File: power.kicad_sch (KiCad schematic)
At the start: 20 parts, among them J3 Life Makes Lemonade, J4 Conn_02x02_Odd_Even, U11 TPS62913, U12 TPS62143RGTR, U13 TPS22993

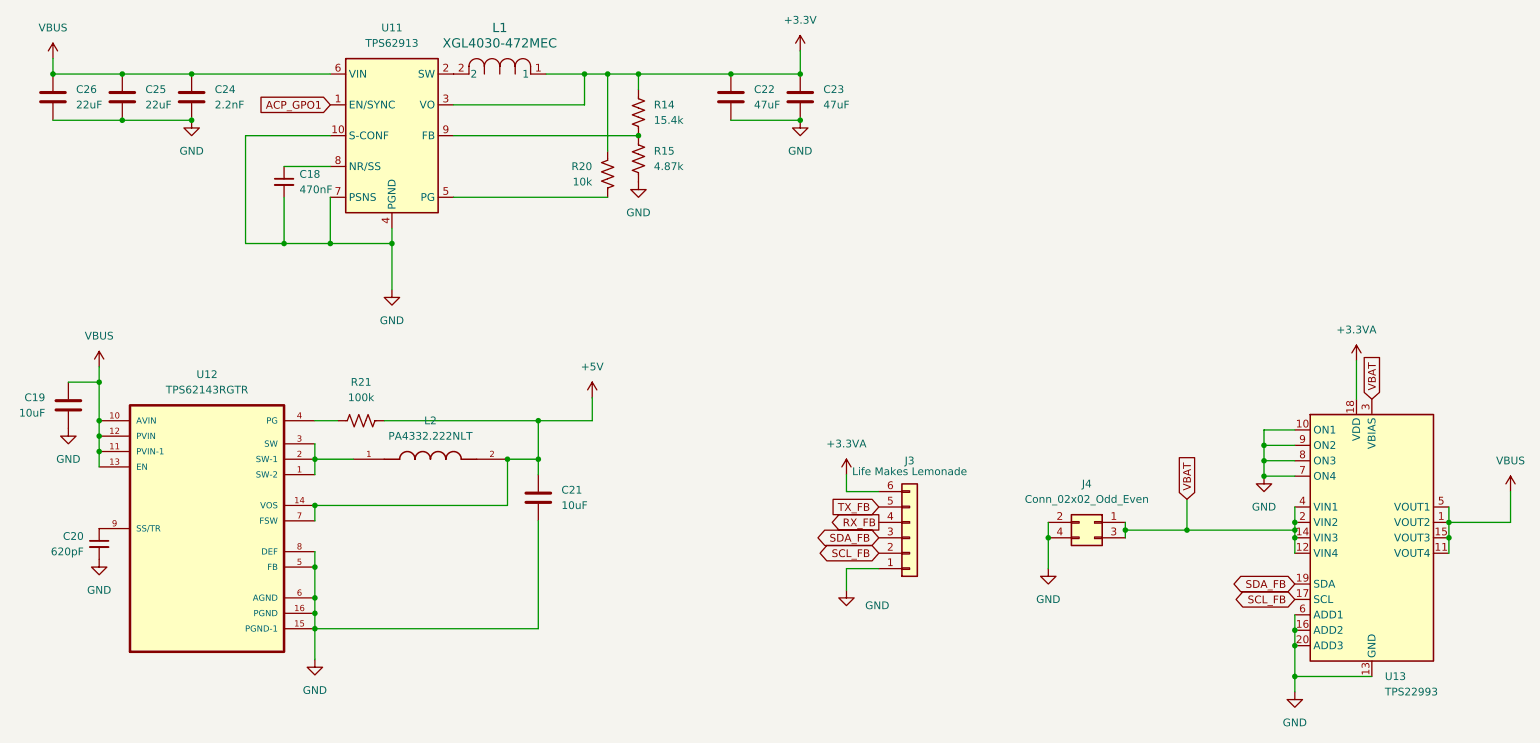
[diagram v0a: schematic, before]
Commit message: changed mounting holes
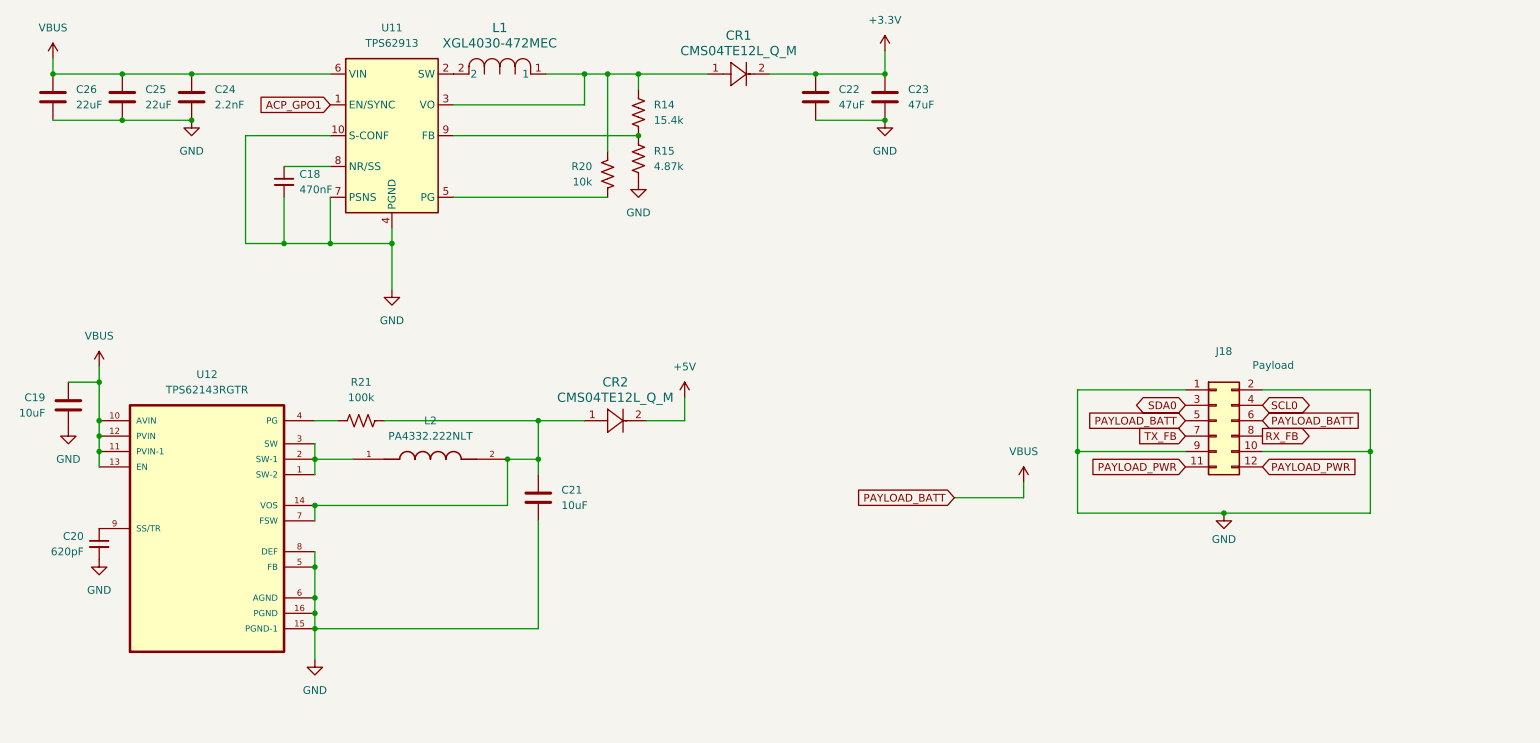
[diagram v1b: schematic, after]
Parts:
- removed J3: Life Makes Lemonade, Connector_PinHeader_2.54mm:PinHeader_1x06_P2.54mm_Vertical, symbol Connector_Generic:Conn_01x06
- removed J4: Conn_02x02_Odd_Even, Connector_Hirose:Hirose_DF11-4DP-2DSA_2x02_P2.00mm_Vertical, symbol Connector_Generic:Conn_02x02_Odd_Even
- removed U13: TPS22993, Package_DFN_QFN:Texas_S-PWQFN-N20, symbol Power_Management:TPS22993
- added CR1, CR2: CMS04TE12L_Q_M, M-FLAT_TOS, symbol CMS04(TE12L,Q,M):CMS04TE12L_Q_M
- added J18: Payload, Connector_Hirose:Hirose_DF11-12DP-2DSA_2x06_P2.00mm_Vertical, symbol Connector_Generic:Conn_02x06_Odd_Even
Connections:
- net +3.3V: now also CR1.2; no longer L1.1, R14.1, R20.1, U11.3 (VO)
- net +5V: now also CR2.2; no longer C21.1, L2.2, R21.2, U12.14 (VOS), U12.7 (FSW)
- net GND: now also J18.1 (Pin_1), J18.10 (Pin_10), J18.2 (Pin_2), J18.9 (Pin_9)
- net RX_FB: now also J18.8 (Pin_8)
- net TX_FB: now also J18.7 (Pin_7)
- net VBUS: now also J18.5 (Pin_5), J18.6 (Pin_6)
- new net: CR1.1, L1.1, R14.1, R20.1, U11.3 (VO)
- new net: C21.1, CR2.1, L2.2, R21.2, U12.14 (VOS), U12.7 (FSW)
- new net PAYLOAD_PWR: J18.11 (Pin_11), J18.12 (Pin_12)
- new net SCL0: J18.4 (Pin_4)
- new net SDA0: J18.3 (Pin_3)
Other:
- moved on the sheet: C22, C23
